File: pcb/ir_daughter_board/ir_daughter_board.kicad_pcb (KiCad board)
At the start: 2 copper layers, 60 x 36 mm, 44 parts, among them IC1 TS2596SCS, J1 USB_OTG, J2 Conn_01x12, J3 Conn_01x12, SW1 BOOT, SW2 RESET, U1 MCP2200T-I/SS, U2 ESP32-WROOM-32E_(16MB), Y1 Crystal

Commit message: minor editorial changes
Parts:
- Y1: value Crystal -> 12,0000-HC49-SMD
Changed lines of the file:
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@@
       (effects (font (size 1 1) (thickness 0.15)))
     )
-    (fp_text value "Crystal" (at 0 3.55 90) (layer "F.Fab")
+    (fp_text value "12,0000-HC49-SMD" (at 0 3.55 90) (layer "F.Fab")
       (effects (font (size 1 1) (thickness 0.15)))
     )

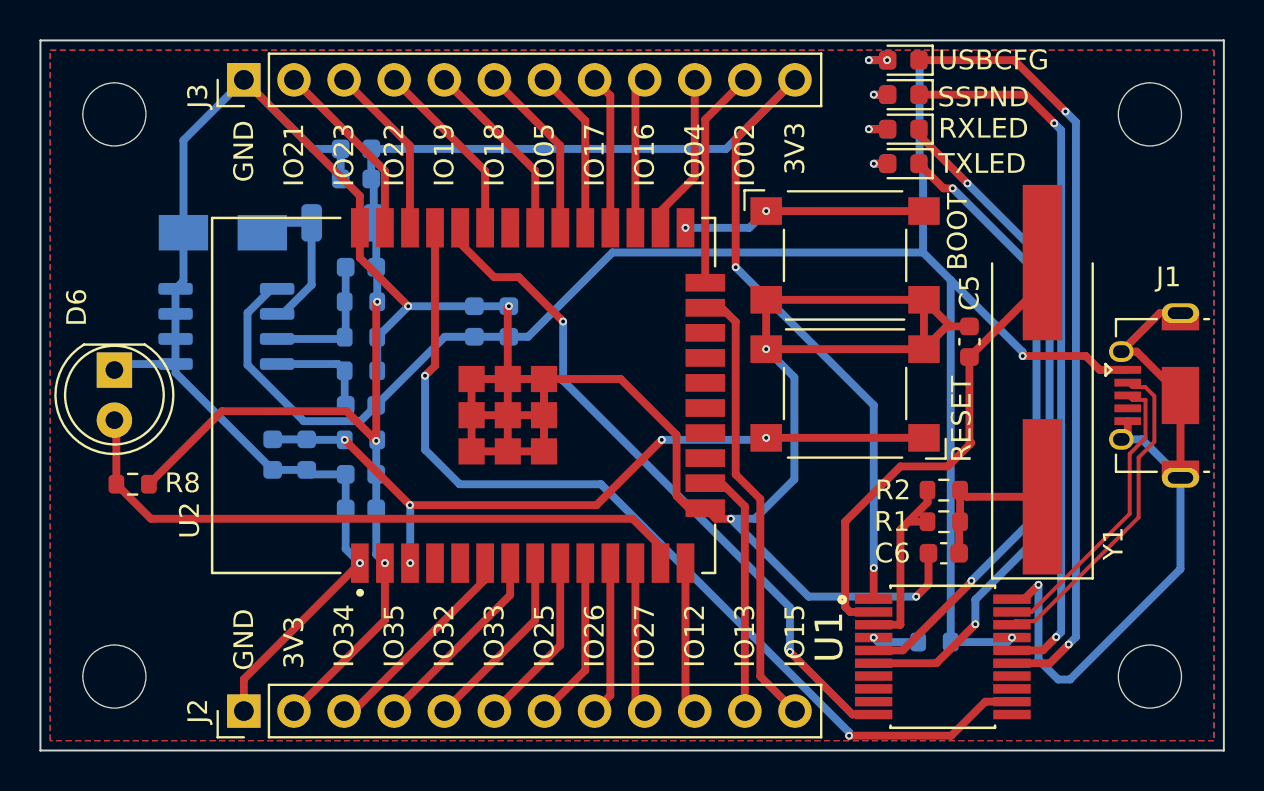
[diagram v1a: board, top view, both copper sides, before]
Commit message: refined circuit with reddit comments
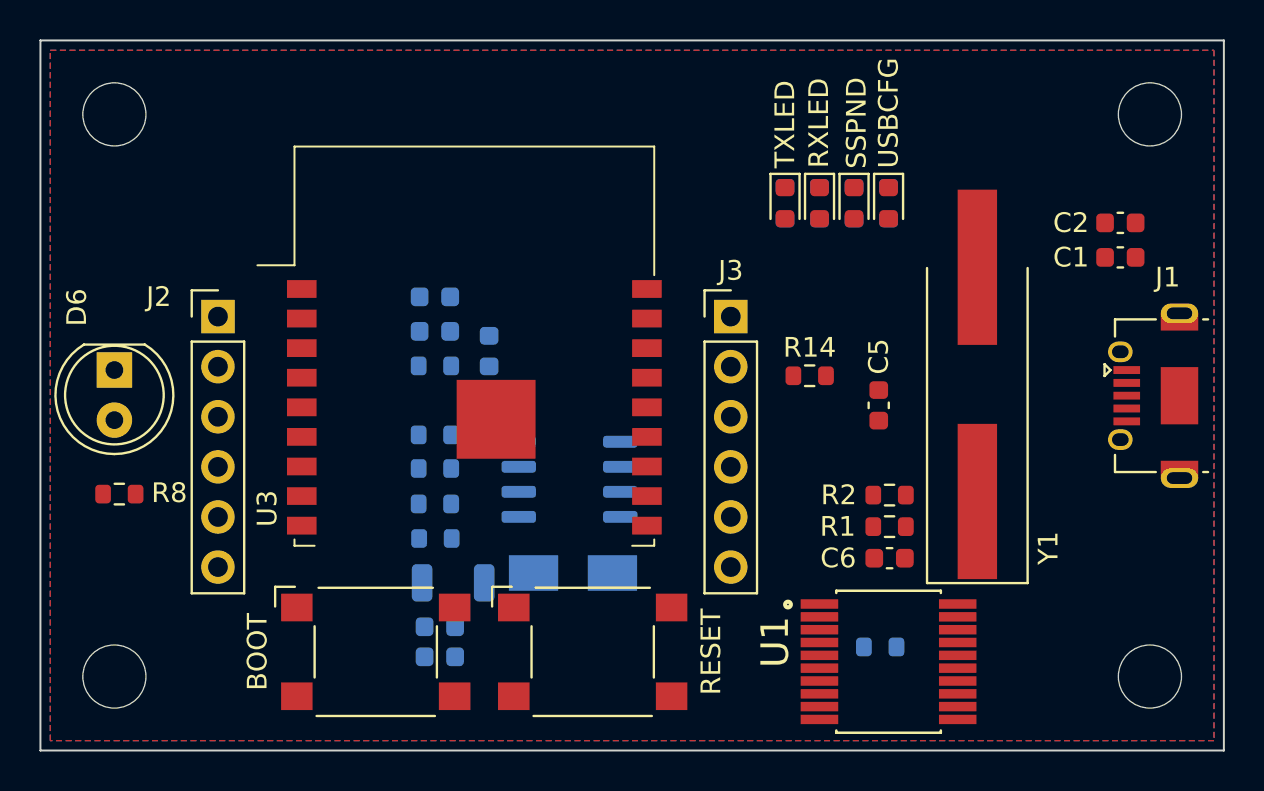
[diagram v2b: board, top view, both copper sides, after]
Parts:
- removed C11: 0.1uF, Capacitor_SMD:C_0603_1608Metric
- removed C12: 10nF, Capacitor_SMD:C_0603_1608Metric
- removed C9: 1uF, Capacitor_SMD:C_0603_1608Metric
- removed U2: ESP32-WROOM-32E_(16MB), ESP32-WROOM-32E:MODULE_ESP32-WROOM-32E_(16MB)
- added R13: 1k5, Resistor_SMD:R_0603_1608Metric, B.Cu at (117.0, 102.2)
- added R14: 10k, Resistor_SMD:R_0603_1608Metric, F.Cu at (136.0, 94.0)
- added U3: ESP-WROOM-02, RF_Module:ESP-WROOM-02, F.Cu at (119.0, 95.6)
- C1: value 470uF -> 4.7uF; moved to F.Cu
- C2: moved to F.Cu
- C7: value 22uF -> 10uF
- J2, J3: value Conn_01x12 -> Conn_01x06; footprint Connector_PinHeader_2.54mm:PinHeader_1x12_P2.54mm_Vertical -> Connector_PinHeader_2.54mm:PinHeader_1x06_P2.54mm_Vertical
- R11: value 2k5 -> 1k
- R9: value 100R -> 10k
- moved C2 33.1 mm to (151.8, 86.2), turned to 180 degrees
- moved C1 31.2 mm to (151.8, 88.0), turned to 180 degrees
- moved SW1 31.1 mm to (114.0, 108.0)
- moved J3 27.4 mm to (132.0, 91.0), turned to 0 degrees
- moved C4 26.1 mm to (117.2, 108.2), turned to 0 degrees
- moved D1 24.8 mm to (124.0, 104.0), turned to 0 degrees
- moved C3 23.1 mm to (117.2, 106.7), turned to 0 degrees
- moved J2 20.0 mm to (106.0, 91.0), turned to 0 degrees
- moved L1 19.1 mm to (117.9, 104.5), turned to 180 degrees
- moved IC1 19.0 mm to (123.8, 99.2), turned to 0 degrees
- moved SW2 18.3 mm to (125.0, 108.0), turned to 0 degrees
- moved C7 11.4 mm to (117.0, 90.0), turned to 0 degrees
- moved R11 10.9 mm to (117.0, 100.5), turned to 0 degrees
- moved C10 10.6 mm to (119.8, 92.8), turned to 90 degrees
- moved C8 8.16 mm to (117.0, 91.8), turned to 0 degrees
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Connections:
- net BOOT renamed Net-(U3-Pad8)
- net OSC1 renamed Net-(C5-Pad1)
- net OSC2 renamed Net-(R1-Pad1)
- net SW_OUTPUT renamed Net-(D1-Pad1)
- net USB_D+ renamed /USB_to_UART/USB_D+
- net USB_D- renamed /USB_to_UART/USB_D-
- C1 pad 1: VCC_USB -> +5V
- C10 pad 1: EN -> Net-(U3-Pad2)
- C2 pad 1: VCC_USB -> +5V
- C3 pad 1: VCC_3V3 -> +3V3
- C4 pad 1: VCC_3V3 -> +3V3
- C7 pad 1: VCC_3V3 -> +3V3
- C8 pad 1: VCC_3V3 -> +3V3
- IC1 pad 1: VCC_USB -> +5V
- IC1 pad 3: FEEDBACK -> Net-(IC1-Pad3)
- J1 pad 1: VCC_USB -> +5V
- J1 pad 6: GND -> unconnected-(J1-Pad6)
- J2 pad 2: VCC_3V3 -> GPIO 05
- J2 pad 3: GPIO 34 -> GPIO 04
- J2 pad 4: GPIO 35 -> GPIO 02
- J2 pad 5: GPIO 32 -> ADC
- J2 pad 6: GPIO 33 -> +3V3
- J3 pad 2: GPIO 23 -> IR
- J3 pad 3: GPIO 22 -> GPIO 16
- J3 pad 4: GPIO 21 -> GPIO 13
- J3 pad 5: GPIO 19 -> GPIO 12
- J3 pad 6: GPIO 18 -> +3V3
- L1 pad 2: VCC_3V3 -> +3V3
- R11 pad 1: VCC_3V3 -> +3V3
- R11 pad 2: FEEDBACK -> Net-(R11-Pad2)
- R12 pad 1: FEEDBACK -> GND
- R12 pad 2: GND -> Net-(IC1-Pad3)
- R3 pad 1: VCC_USB -> +5V
- R4 pad 1: VCC_USB -> +3V3
- R5 pad 2: VCC_USB -> +3V3
- R6 pad 1: VCC_USB -> +3V3
- R7 pad 2: VCC_USB -> +3V3
- R8 pad 2: VCC_3V3 -> +3V3
- R9 pad 1: EN -> Net-(U3-Pad2)
- R9 pad 2: VCC_3V3 -> +3V3
- SW2 pad 1: EN -> Net-(U3-Pad15)
- SW2 pad 2: EN -> Net-(U3-Pad15)
- U1 pad 1: VCC_3V3 -> +3V3
- U1 pad 10: TXD -> /IR_Remote_Circuit/RXD
- U1 pad 12: RXD -> /IR_Remote_Circuit/TXD
- U1 pad 17: VCC_USB -> +3V3
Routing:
- net GND: track 203.6 -> 0.00 mm, vias 7 -> 0
- net VCC_3V3: track 97.9 -> 0.00 mm, vias 5 -> 0
- net VCC_USB: track 87.9 -> 0.00 mm, vias 2 -> 0
- net RXD: track 48.0 -> 0.00 mm, vias 2 -> 0
- net USBCFG: track 39.2 -> 0.00 mm, vias 2 -> 0
- net EN: track 38.8 -> 0.00 mm, vias 5 -> 0
- net SSPND: track 36.3 -> 0.00 mm, vias 2 -> 0
- net RXLED: track 35.4 -> 0.00 mm, vias 2 -> 0
- net TXD: track 34.7 -> 0.00 mm, vias 2 -> 0
- net IR: track 33.0 -> 0.00 mm
- net TXLED: track 31.9 -> 0.00 mm, vias 2 -> 0
- net Net-(C5-Pad1): track 24.7 -> 0.00 mm
- net GPIO 15: track 22.8 -> 0.00 mm
- net /USB_to_UART/USB_D-: track 16.8 -> 0.00 mm
- net /USB_to_UART/USB_D+: track 15.1 -> 0.00 mm
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
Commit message: updated schematic
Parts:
- removed C3: 470uF, Capacitor_SMD:C_0603_1608Metric
- removed D1: SK34A, Diode_SMD:D_SMA
- removed R12: 1k5, Resistor_SMD:R_0603_1608Metric
- C1: value 4.7uF -> 10uF; moved to B.Cu
- C2: value 0.1uF -> 18pF; moved to B.Cu
- C4: value 0.1uF -> 10uF
- C5, C6, D6, J1, R1, R14, R2, R8, U1, Y1: moved to B.Cu
- IC1: value TS2596SCS -> NCP1521BSN; footprint Package_SO:SO-8_3.9x4.9mm_P1.27mm -> Package_SO:TSOP-5_1.65x3.05mm_P0.95mm
- L1: value 33uH -> 2.2uH
- R10: value 100k -> 1k
- R11: value 1k -> 4k3
- R13: value 1k5 -> 200R
- moved C1 49.5 mm to (106.8, 108.7), turned to -90 degrees
- moved C2 41.0 mm to (116.4, 107.0)
- moved R14 37.7 mm to (99.2, 102.1), turned to 90 degrees
- moved R3 37.6 mm to (102.4, 102.1), turned to 90 degrees
- moved U1 30.8 mm to (113.2, 93.3), turned to 90 degrees
- moved D4 29.5 mm to (127.1, 111.8), turned to 0 degrees
- moved D5 27.1 mm to (127.1, 110.0), turned to 0 degrees
- moved Y1 26.2 mm to (119.4, 101.8), turned to 180 degrees
- moved D3 24.8 mm to (127.1, 108.2), turned to 0 degrees
- moved D2 22.6 mm to (127.1, 106.5), turned to 0 degrees
- moved R6 21.7 mm to (118.7, 89.3), turned to 0 degrees
- moved C5 21.4 mm to (118.2, 96.5)
- moved C6 21.3 mm to (119.8, 96.5), turned to -90 degrees
- moved R7 20.4 mm to (118.7, 90.9), turned to 180 degrees
- moved R1 19.4 mm to (121.4, 96.5), turned to -90 degrees
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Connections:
- C2 pad 1: +5V -> +3V3
- C2 pad 2: GND -> Net-(C2-Pad2)
- D4 pad 1: USBCFG -> GND
- D5 pad 1: SSPND -> GND
- D6 pad 1: GND -> IR
- D6 pad 2: IR -> Net-(D6-Pad2)
- IC1 pad 2: Net-(D1-Pad1) -> GND
- IC1 pad 3: Net-(IC1-Pad3) -> +5V
- IC1 pad 4: Net-(IC1-Pad4) -> Net-(C2-Pad2)
- IC1 pad 5: GND -> Net-(IC1-Pad5)
- J2 pad 2: GPIO 05 -> IR
- J2 pad 3: GPIO 04 -> GPIO 12
- J2 pad 4: GPIO 02 -> GPIO 13
- J2 pad 5: ADC -> GPIO 02
- J3 pad 2: IR -> GPIO 16
- J3 pad 3: GPIO 16 -> ADC
- J3 pad 4: GPIO 13 -> GPIO 05
- J3 pad 5: GPIO 12 -> GPIO 04
- L1 pad 1: Net-(D1-Pad1) -> Net-(IC1-Pad5)
- R10 pad 1: Net-(IC1-Pad4) -> Net-(C2-Pad2)
- R13 pad 2: Net-(IC1-Pad3) -> Net-(C2-Pad2)
- R6 pad 1: +3V3 -> USBCFG
- R7 pad 2: +3V3 -> SSPND
- R8 pad 1: IR -> Net-(D6-Pad2)
- U1 pad 11: unconnected-(U1-Pad11) -> /USB_to_UART/RTS
- U1 pad 13: unconnected-(U1-Pad13) -> /USB_to_UART/CTS
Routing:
- net GND: track 0.00 -> 133.2 mm, vias 0 -> 5
- net +3V3: track 0.00 -> 92.5 mm, vias 0 -> 3
- net +5V: track 0.00 -> 48.6 mm, vias 0 -> 3
- net Net-(D4-Pad2): track 0.00 -> 42.0 mm, vias 0 -> 1
- net Net-(D5-Pad2): track 0.00 -> 40.0 mm, vias 0 -> 1
- net Net-(SW2-Pad1): track 0.00 -> 33.8 mm
- net /USB_to_UART/USB_D+: track 0.00 -> 28.1 mm
- net /USB_to_UART/USB_D-: track 0.00 -> 27.0 mm
- net /IR_Remote_Circuit/TXD: track 0.00 -> 23.3 mm, vias 0 -> 1
- net RXLED: track 0.00 -> 20.2 mm, vias 0 -> 1
- net /IR_Remote_Circuit/RXD: track 0.00 -> 19.9 mm, vias 0 -> 1
- net TXLED: track 0.00 -> 17.6 mm, vias 0 -> 1
- net Net-(R3-Pad2): track 0.00 -> 17.1 mm
- net Net-(SW1-Pad1): track 0.00 -> 16.5 mm
- net Net-(R14-Pad2): track 0.00 -> 13.6 mm, vias 0 -> 1
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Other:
- board size 60 x 36 mm -> 45 x 32 mm

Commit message: change MCP2200 footprint to standard footprint
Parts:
- U1: footprint MCP2200T-I_SS:SOP65P780X200-20N -> Package_SO:SSOP-20_5.3x7.2mm_P0.65mm
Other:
- outline, holes or cut-outs redrawn

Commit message: minor update in PCB
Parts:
- added C3: 100nF, Capacitor_SMD:C_0603_1608Metric, B.Cu at (123.5, 108.8)
- C10, C8: value 0.1uF -> 100nF
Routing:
- net /USB_to_UART/USB_D+: track 28.1 -> 26.5 mm
- net +3V3: track 92.5 -> 94.0 mm
- net GND: track 133.2 -> 134.6 mm

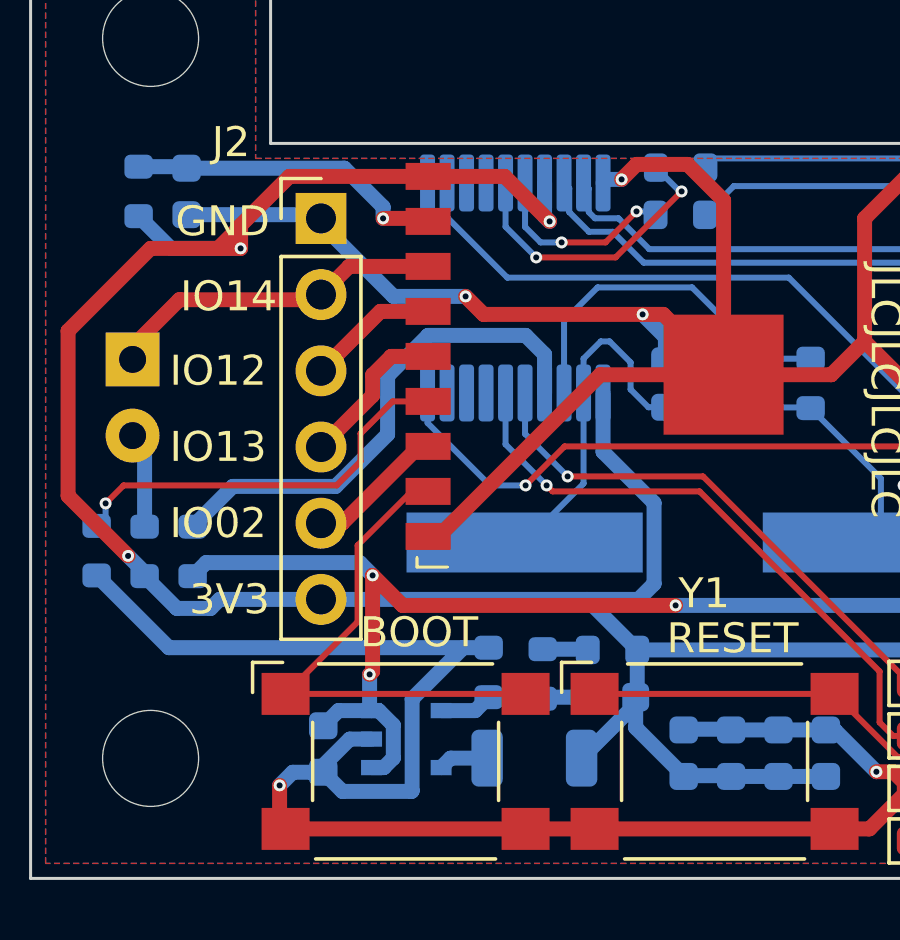
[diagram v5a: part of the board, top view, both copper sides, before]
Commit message: adapted pcb due to parts availability
Signed-off-by: LehrChristoph <christoph.lehr@gmx.at>
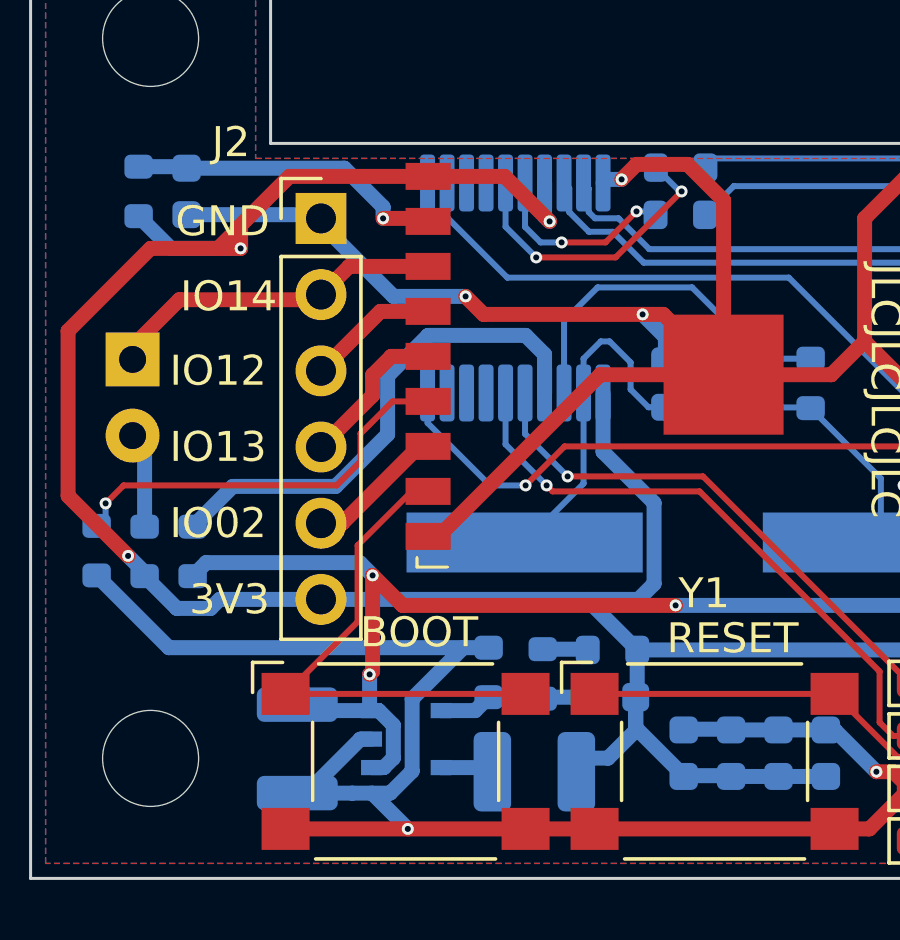
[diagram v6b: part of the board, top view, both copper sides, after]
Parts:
- C1: value 10uF -> 4.7uF; footprint Capacitor_SMD:C_0603_1608Metric -> Capacitor_SMD:C_1210_3225Metric
- L1: footprint Inductor_SMD:L_1206_3216Metric -> Inductor_SMD:L_1210_3225Metric
- moved C1 0.87 mm to (105.9, 108.7)
- moved L1 0.45 mm to (113.8, 109.4)
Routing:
- net +3V3: track 94.0 -> 94.5 mm

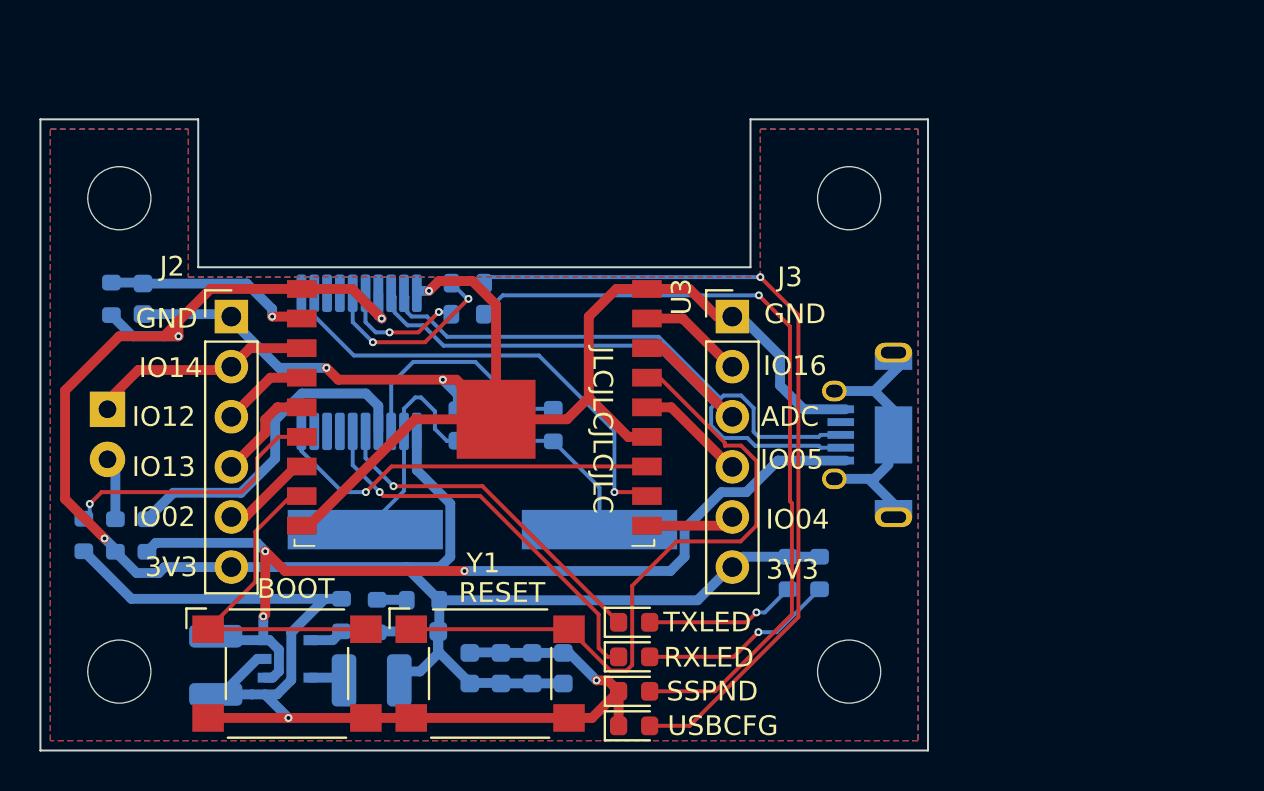
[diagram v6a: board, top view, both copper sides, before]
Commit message: minor updateds in references and values
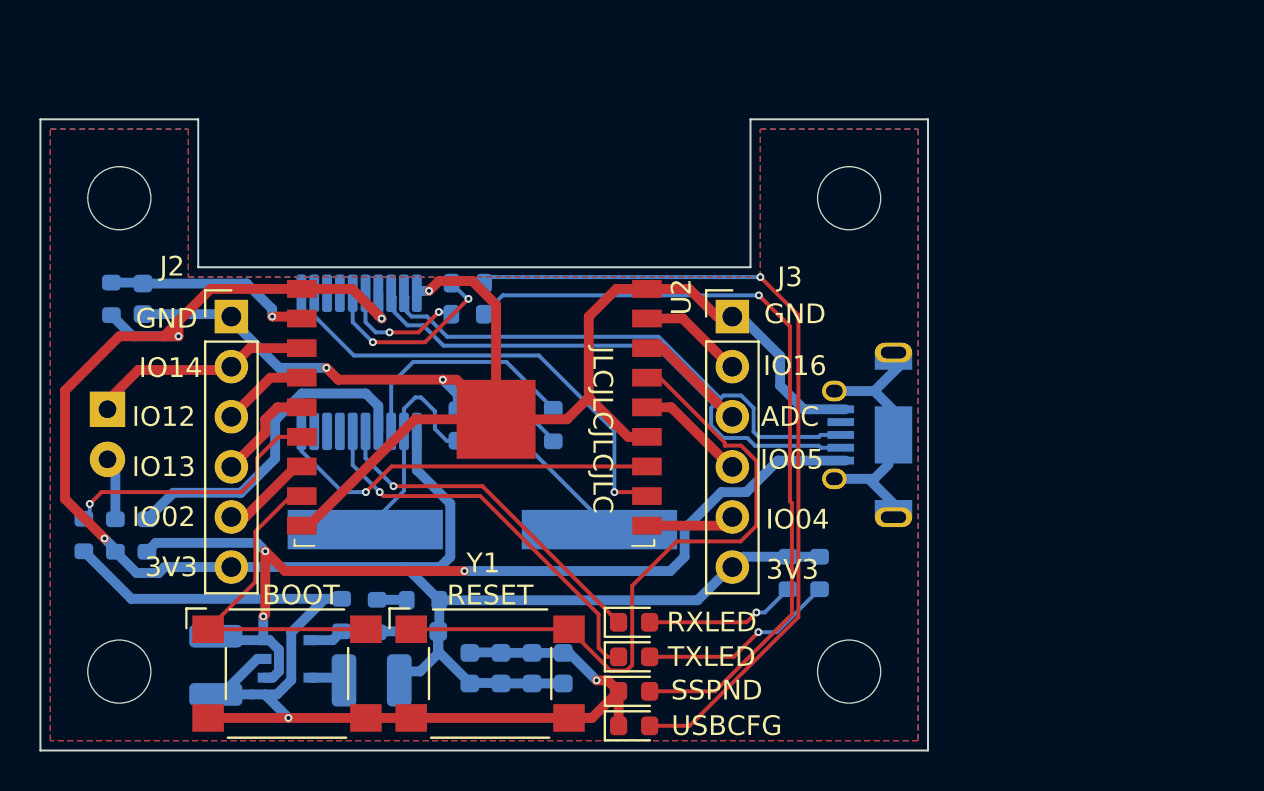
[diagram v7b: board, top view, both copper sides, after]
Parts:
- D1: renamed from D2; value TXLED -> LED
- D2: renamed from D3; value RXLED -> LED
- D3: renamed from D4; value USBCFG -> LED
- D4: renamed from D5; value SSPND -> LED
- D5: renamed from D6; value LTE-5208A -> IR-LED 940nm
- R4: renamed from R1; value 1k1 -> 430R
- R5: renamed from R2; value 750R -> 12R
- SW1: renamed from SW2; value RESET -> SW_MEC_5E
- SW2: renamed from SW1; value BOOT -> SW_MEC_5E
- renumbered C4 to C3, C5 to C4, C6 to C5, C3 to C6, C10 to C7, C7 to C8, C8 to C9, R11 to R1, R7 to R10, R9 to R11, R14 to R12, R8 to R13, R13 to R2, R10 to R3, R3 to R6, R4 to R7, R5 to R8, R6 to R9, U3 to U2
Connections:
- C5 pad 2: Net-(C6-Pad2) -> Net-(R4-Pad2)
- R4 pad 1: Net-(R1-Pad1) -> Net-(R5-Pad2)
- R4 pad 2: Net-(C6-Pad2) -> Net-(R4-Pad2)
- R5 pad 1: Net-(R1-Pad1) -> Net-(R5-Pad1)
- R5 pad 2: Net-(C6-Pad2) -> Net-(R5-Pad2)
- U1 pad 3: Net-(R1-Pad1) -> Net-(R5-Pad1)
- Y1 pad 1: Net-(C6-Pad2) -> Net-(R4-Pad2)
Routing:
- net Net-(R5-Pad1): track 0.00 -> 12.1 mm
- net Net-(R1-Pad1): track 12.0 -> 0.00 mm
- net Net-(C6-Pad2): track 8.60 -> 0.00 mm
- net Net-(R4-Pad2): track 0.00 -> 7.71 mm
- net Net-(R5-Pad2): track 0.00 -> 2.34 mm
